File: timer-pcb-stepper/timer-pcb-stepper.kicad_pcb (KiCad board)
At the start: 4 copper layers, 130 x 148.5 mm, 18 parts, among them J1 JST_05, J2 JST_05, J3 JST_05, U1 ULN2003, U3 ULN2003, U4 ULN2003

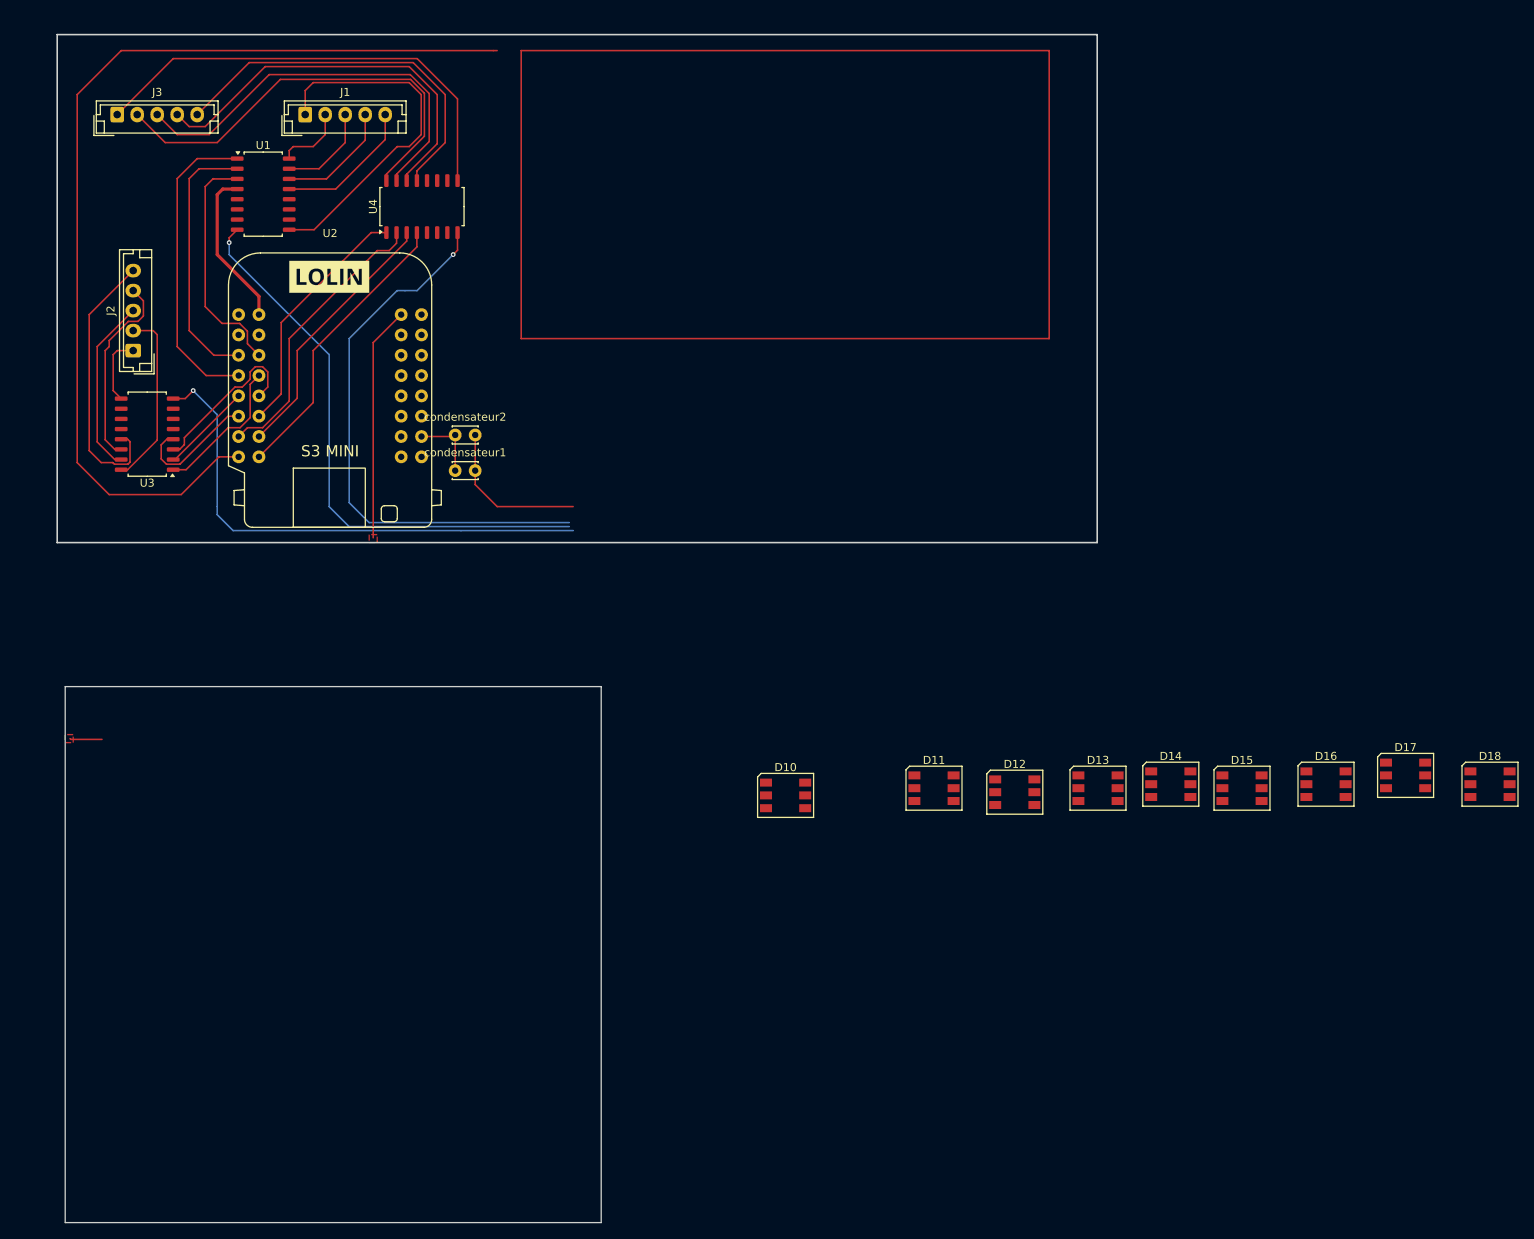
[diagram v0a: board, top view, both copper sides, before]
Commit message: mise à jour des fichiers kicad PCB-led et PCB-stepper. circuit imprimé plus propre et ajout de connecteur jst
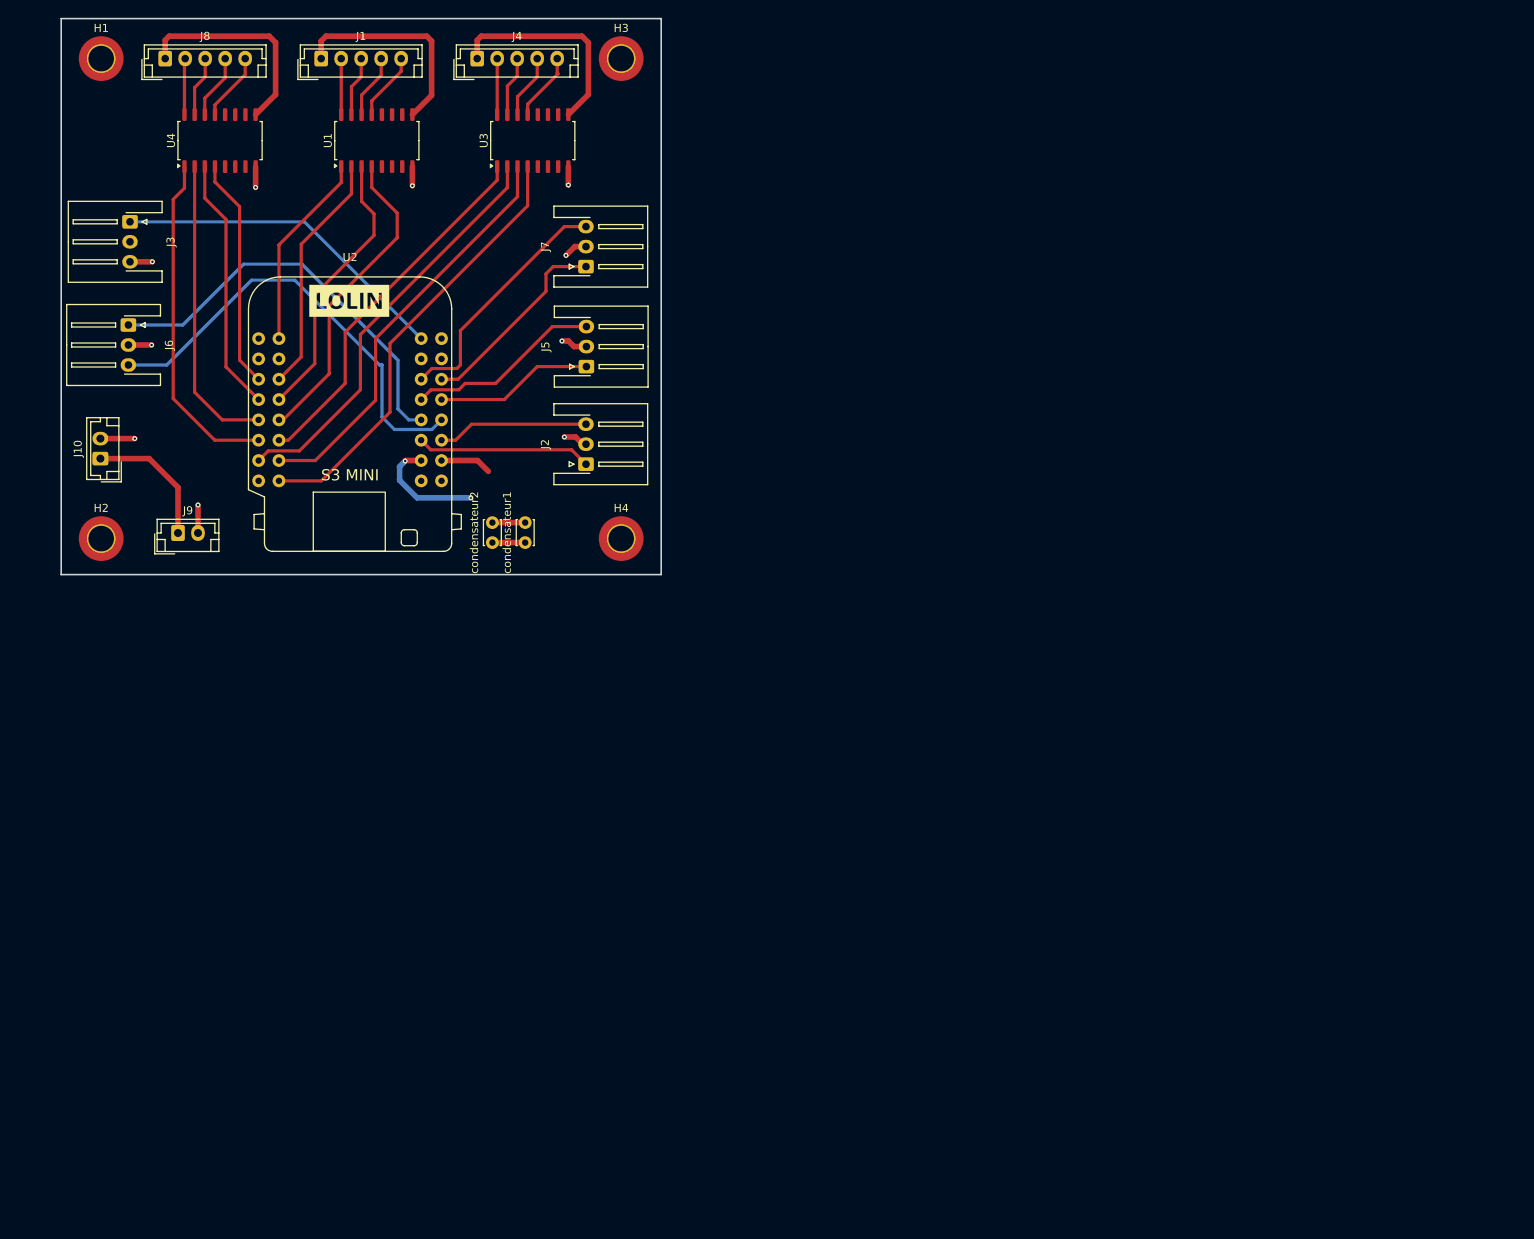
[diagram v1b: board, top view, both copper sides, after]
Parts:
- removed D10, D11, D12, D13, D14, D15, D16, D17, D18: WS2812, LED_SMD:LED_WS2812_PLCC6_5.0x5.0mm_P1.6mm
- added G***: LOGO, image.preety:portfolioQR, B.Cu at (100.6, 59.8)
- added H1: MountingHole, MountingHole:MountingHole_3.2mm_M3_DIN965_Pad_TopOnly, F.Cu at (55.0, 45.0)
- added H2: MountingHole, MountingHole:MountingHole_3.2mm_M3_DIN965_Pad_TopOnly, F.Cu at (55.0, 105.0)
- added H3: MountingHole, MountingHole:MountingHole_3.2mm_M3_DIN965_Pad_TopOnly, F.Cu at (120.0, 45.0)
- added H4: MountingHole, MountingHole:MountingHole_3.2mm_M3_DIN965_Pad_TopOnly, F.Cu at (120.0, 105.0)
- added J10: JST_02, Connector_JST:JST_EH_B2B-EH-A_1x02_P2.50mm_Vertical, F.Cu at (54.9, 95.0)
- added J2: JST_03, Connector_JST:JST_XH_S3B-XH-A-1_1x03_P2.50mm_Horizontal, F.Cu at (115.6, 95.7)
- added J3: JST_03_Led_panel, Connector_JST:JST_XH_S3B-XH-A-1_1x03_P2.50mm_Horizontal, F.Cu at (58.6, 65.4)
- added J5: JST_03, Connector_JST:JST_XH_S3B-XH-A-1_1x03_P2.50mm_Horizontal, F.Cu at (115.7, 83.5)
- added J6: JST_03, Connector_JST:JST_XH_S3B-XH-A-1_1x03_P2.50mm_Horizontal, F.Cu at (58.4, 78.3)
- added J7: JST_03, Connector_JST:JST_XH_S3B-XH-A-1_1x03_P2.50mm_Horizontal, F.Cu at (115.6, 71.0)
- added J9: JST_02, Connector_JST:JST_EH_B2B-EH-A_1x02_P2.50mm_Vertical, F.Cu at (64.6, 104.3)
- moved U3 60.6 mm to (108.9, 55.2), turned to 90 degrees
- moved J4 56.4 mm to (102.0, 45.0), turned to 0 degrees
- moved U4 26.6 mm to (69.9, 55.2)
- moved U1 15.7 mm to (89.5, 55.2), turned to 90 degrees
- moved condensateur2 14.2 mm to (103.9, 105.5), turned to 90 degrees
- moved condensateur1 12.6 mm to (108.0, 105.5), turned to 90 degrees
- moved J8 9.22 mm to (63.0, 45.0)
- moved J1 7.28 mm to (82.5, 45.0)
- moved U2 3.91 mm to (86.1, 88.9)
- renumbered J2 to J4, J3 to J8
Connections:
- U2 pad 10: M2C -> M1D
- U2 pad 11: M2D -> M3A
- U2 pad 12: M3A -> M2A
- U2 pad 13: M3B -> M2B
- U2 pad 14: M3C -> M2C
- U2 pad 16: M3D -> M2D
- U2 pad 17: WS2812_Med -> WS2812_Led
- U2 pad 2: M1D -> M1A
- U2 pad 5: M1B -> M3D
- U2 pad 6: M1C -> M1B
- U2 pad 7: M1A -> M3C
- U2 pad 8: M2A -> M1C
- U2 pad 9: M2B -> M3B
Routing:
- net GND: track 214.3 -> 50.9 mm, vias 3 -> 11
- net Net-(BT1-+): track 124.6 -> 0.00 mm
- net Switch_motor_1_Down: track 0.00 -> 55.6 mm
- net Switch_motor_1_Up: track 0.00 -> 51.4 mm
- net Net-(U4-O1): track 54.2 -> 7.04 mm
- net Net-(U4-O2): track 51.7 -> 7.55 mm
- net WS2812_Led: track 0.00 -> 42.4 mm
- net Net-(U4-O3): track 50.0 -> 8.06 mm
- net M2B: track 11.5 -> 51.9 mm
- net M2D: track 16.0 -> 55.3 mm
- net Net-(U4-O4): track 47.6 -> 8.57 mm
- net Switch_motor_3_Up: track 0.00 -> 31.3 mm
- net +5V: track 111.3 -> 80.1 mm
- net M2C: track 20.9 -> 51.8 mm
- net WS2812_Med: track 29.3 -> 0.00 mm
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- removed copper zone on F.Cu, net WS2812_Med
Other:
- board size 130 x 148.5 mm -> 75 x 69.5 mm
- board text added: "Merci à Jacques pour son aide"
- board text added: "Premier projet électronique"
- board text added: "Start: 15 févier 2025"
- board text added: "http://thomasfessler.com"
- board text added: "https://www.supcik.net/"

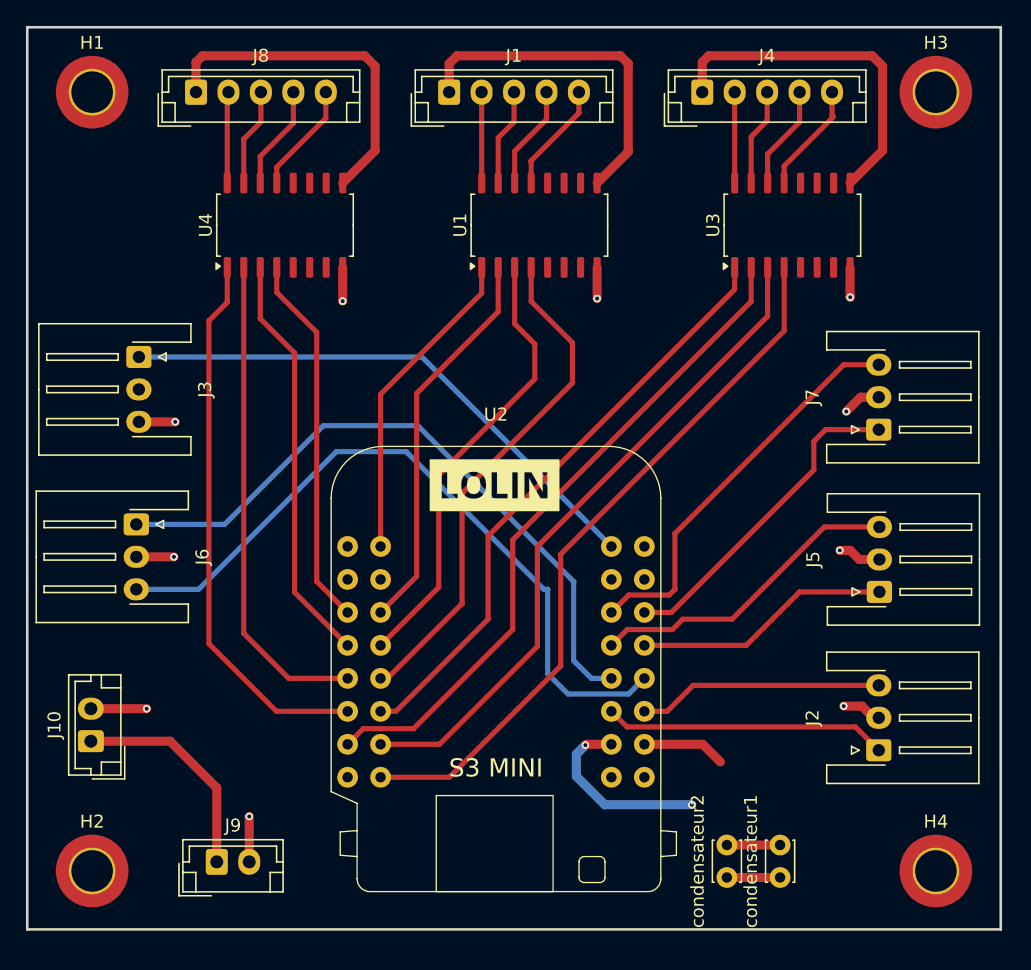
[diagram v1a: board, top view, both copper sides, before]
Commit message: mise à jour des fichiers kicad PCB-stepper. circuit imprimé plus propre et ajout de connecteur jst
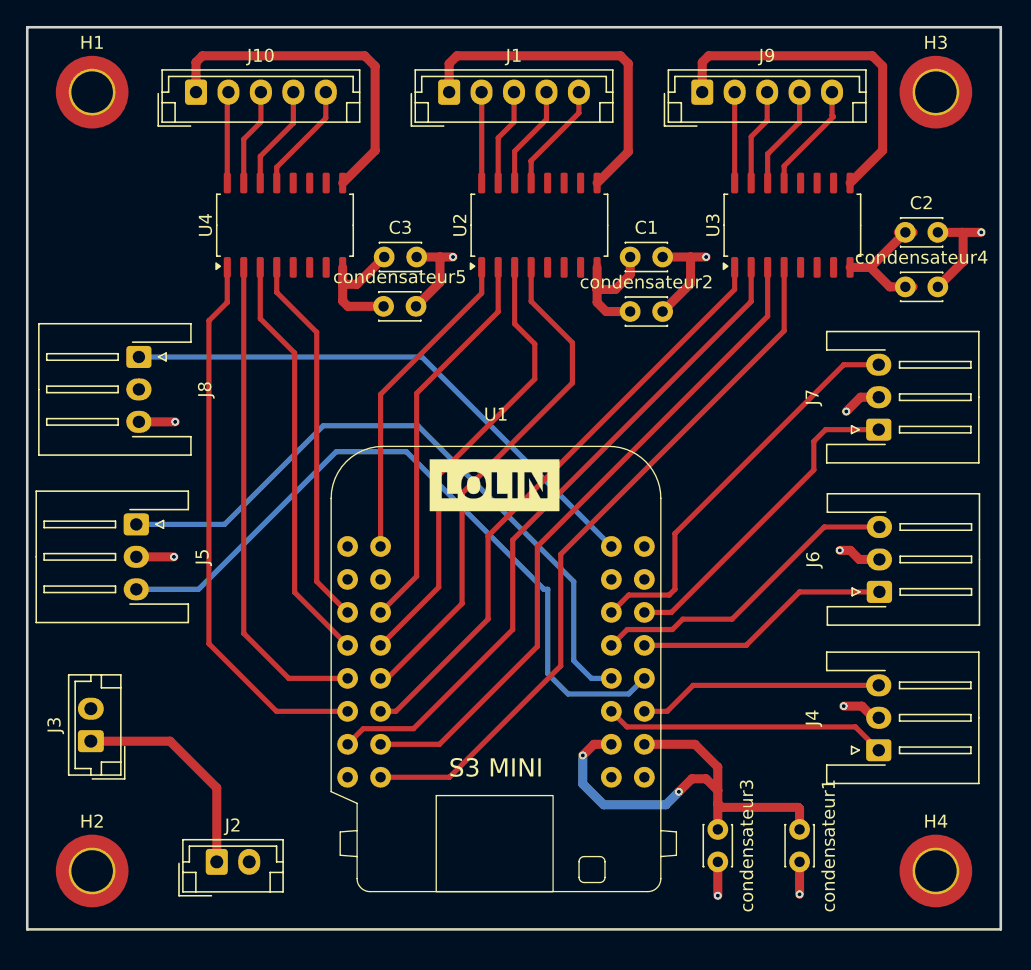
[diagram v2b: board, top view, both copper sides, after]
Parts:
- added C1: 10uF, Capacitor_THT:C_Disc_D3.0mm_W2.0mm_P2.50mm, F.Cu at (96.5, 57.7)
- added C2: 10uF, Capacitor_THT:C_Disc_D3.0mm_W2.0mm_P2.50mm, F.Cu at (117.7, 55.8)
- added C3: 10uF, Capacitor_THT:C_Disc_D3.0mm_W2.0mm_P2.50mm, F.Cu at (77.5, 57.7)
- added condensateur2: 100nF, Capacitor_THT:C_Disc_D3.0mm_W2.0mm_P2.50mm, F.Cu at (96.5, 61.9)
- added condensateur4: 100nF, Capacitor_THT:C_Disc_D3.0mm_W2.0mm_P2.50mm, F.Cu at (117.7, 60.0)
- added condensateur5: 100nF, Capacitor_THT:C_Disc_D3.0mm_W2.0mm_P2.50mm, F.Cu at (77.5, 61.5)
- moved condensateur1 3.99 mm to (109.5, 101.8), turned to -90 degrees
- moved condensateur3 3.77 mm to (103.2, 101.8), turned to -90 degrees
- renumbered J8 to J10, J9 to J2, J10 to J3, J2 to J4, J6 to J5, J5 to J6, J3 to J8, J4 to J9, U2 to U1, U1 to U2, condensateur2 to condensateur3
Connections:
- J3 pad 2: Off -> +5V
- U1 pad 29: GND -> Net-(U1-GND-Pad29)
- U1 pad 30: GND -> Net-(U1-GND-Pad29)
- U2 pad 8: GND -> Net-(U2-GND)
- U3 pad 8: GND -> Net-(U3-GND)
- U4 pad 8: GND -> Net-(U4-GND)
- condensateur1 pad 1: GND -> Net-(U1-GND-Pad29)
- condensateur1 pad 2: Net-(BT1--) -> +5V
- condensateur3 pad 1: GND -> Net-(U1-GND-Pad29)
- condensateur3 pad 2: Net-(BT1--) -> +5V
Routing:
- net Net-(U1-GND-Pad29): track 0.00 -> 36.3 mm, vias 0 -> 2
- net GND: track 50.9 -> 39.4 mm, vias 11 -> 8
- net Net-(U3-GND): track 0.00 -> 11.0 mm
- net Net-(U2-GND): track 0.00 -> 9.92 mm
- net Net-(U4-GND): track 0.00 -> 9.78 mm
- net Off: track 4.30 -> 0.00 mm, vias 1 -> 0
- net Net-(BT1--): track 4.10 -> 5.10 mm
- net +5V: vias 0 -> 2
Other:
- board text added: "Un grand merci à Jacques pour son aide"
- board text removed: "Merci à Jacques pour son aide"
